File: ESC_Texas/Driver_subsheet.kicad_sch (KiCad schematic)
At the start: 24 parts, among them IC10 UCC21331CQDRQ1, Q2 IPD100N06S4, Q5 IPD100N06S4

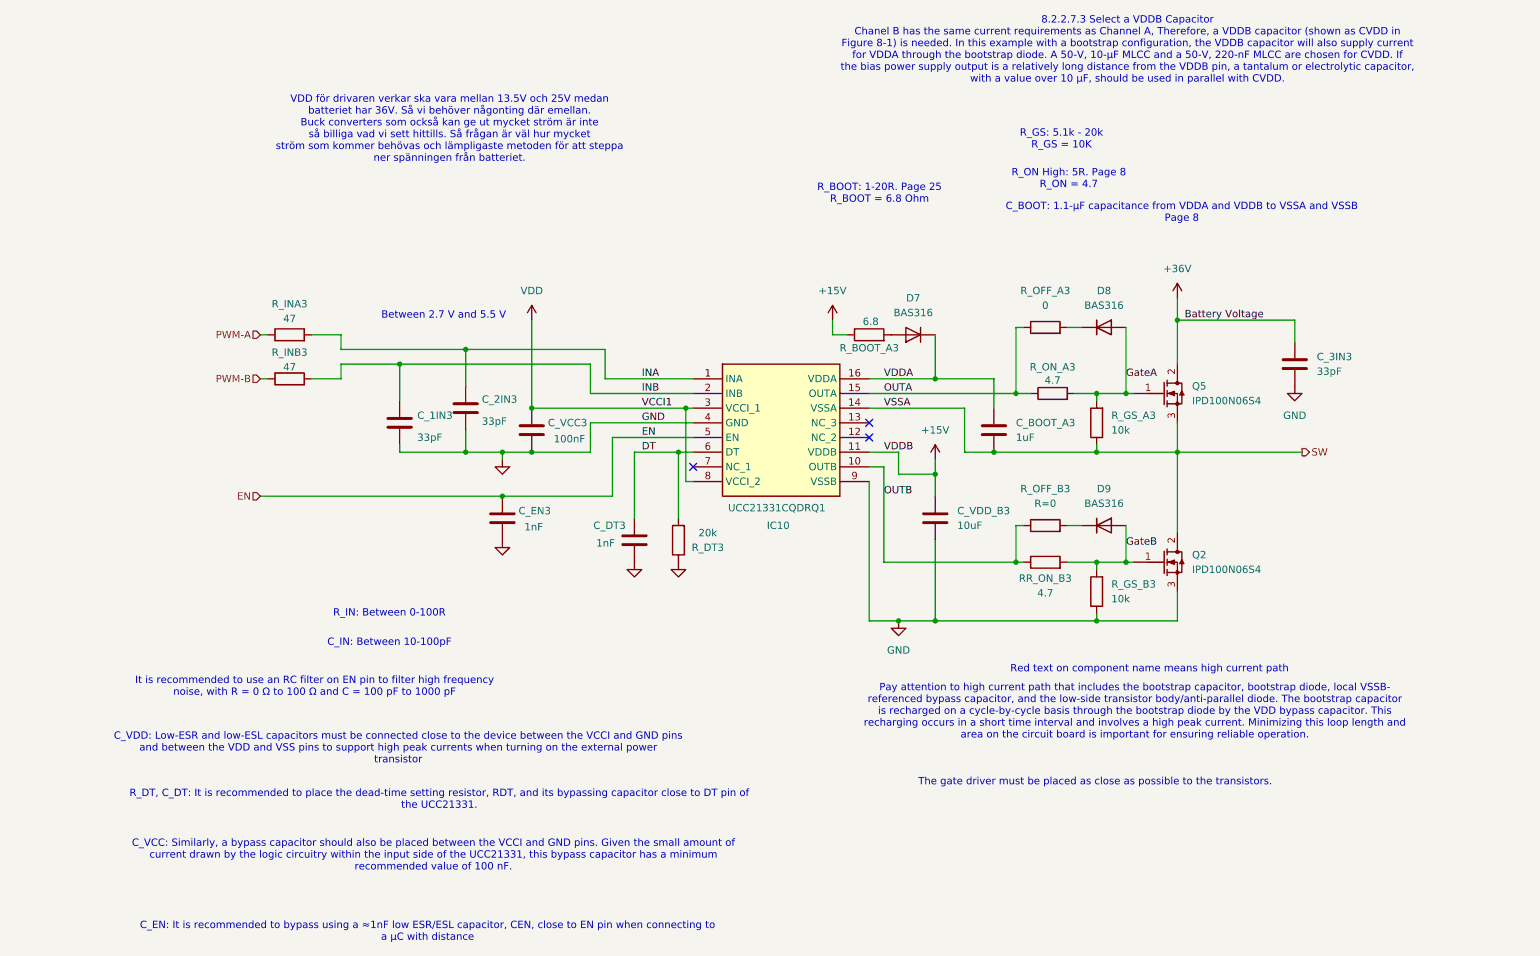
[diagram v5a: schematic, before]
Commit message: Added capacitors and more
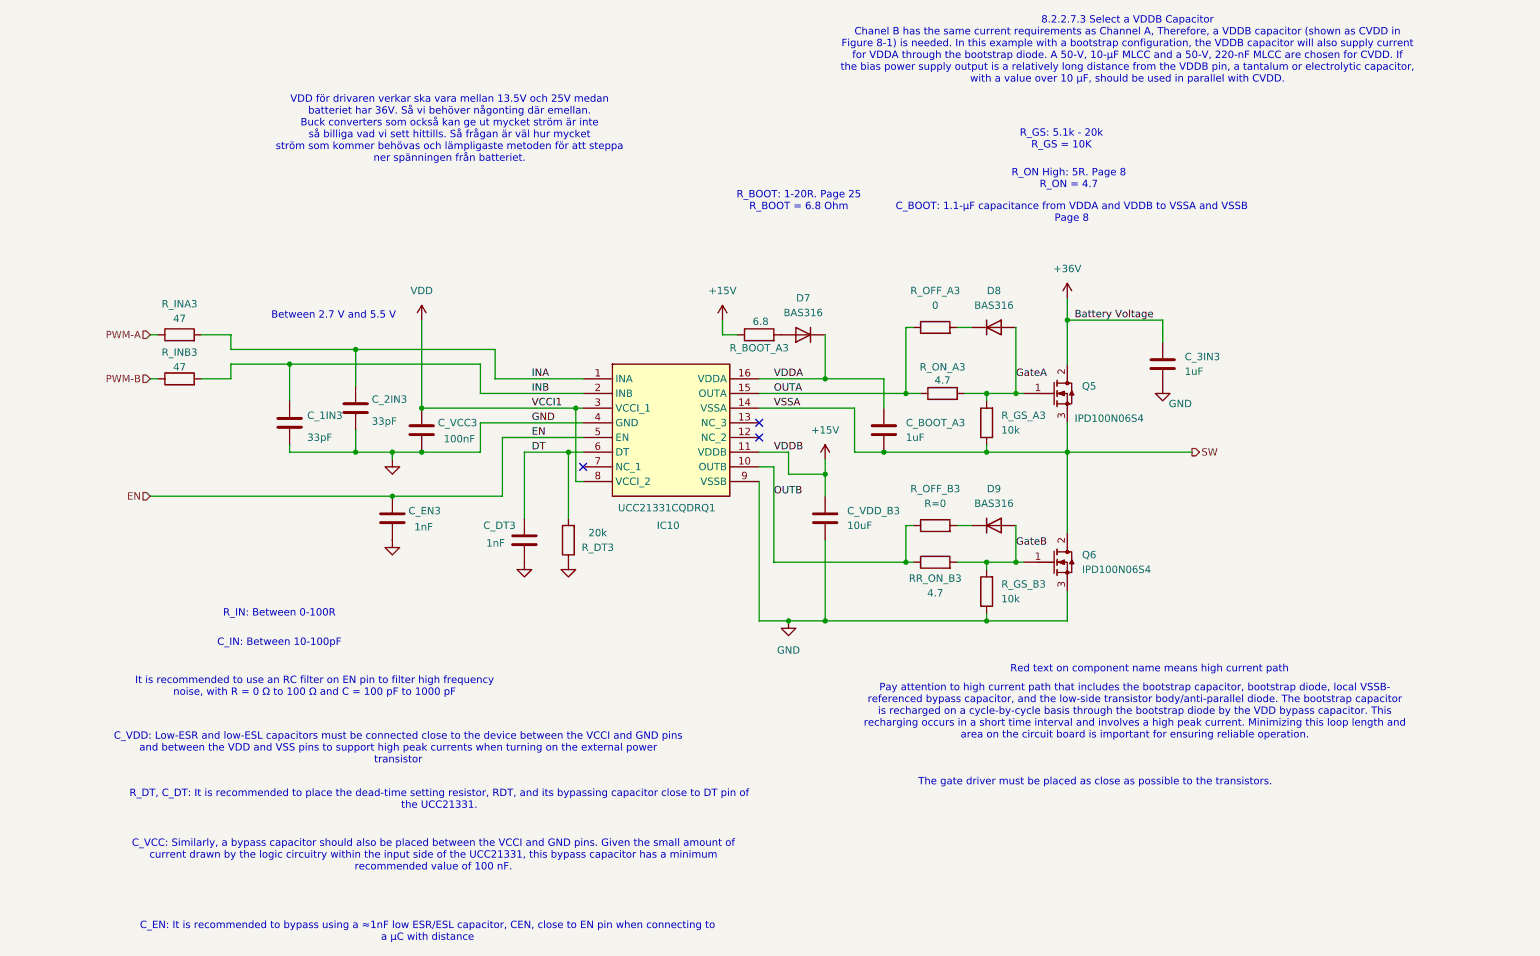
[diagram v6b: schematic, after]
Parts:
- C_3IN3: value 33pF -> 1uF
- renumbered Q2 to Q6
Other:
- moved on the sheet: C_1IN3, C_2IN3, C_3IN3, C_BOOT_A3, C_DT3, C_EN3, C_VCC3, C_VDD_B3, D7, D8, D9, IC10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

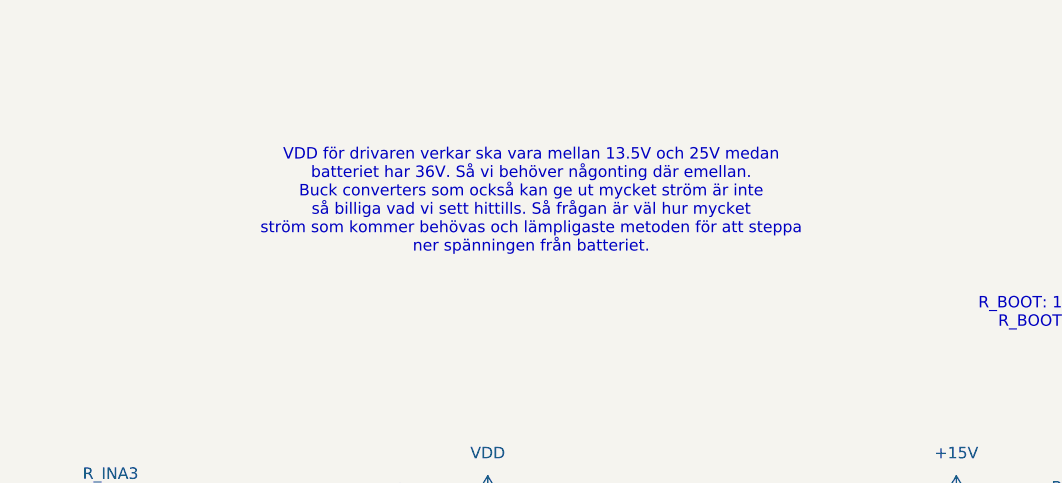
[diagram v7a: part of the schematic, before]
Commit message: Testpoints instead of hearders
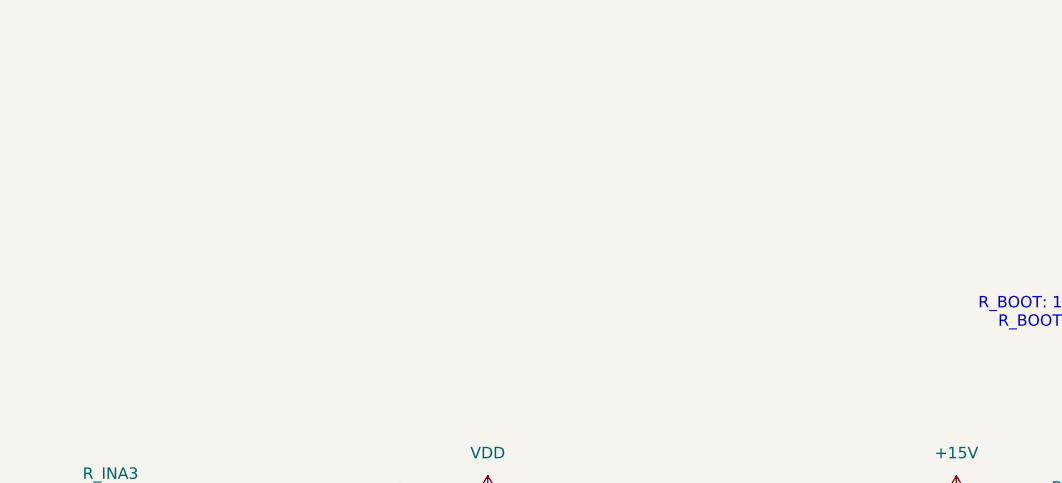
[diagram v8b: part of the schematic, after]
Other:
- note removed: "VDD för drivaren verkar ska vara mellan 13.5V och 25V medan batteriet har 36V. Så vi behöver någonting där emellan. Buck converters som också kan ge ut mycket ström är inte så billiga vad vi sett hittills. Så frågan är väl hur mycket ström som kommer behövas och lämpligaste metoden för att steppa ner spänningen från batteriet."
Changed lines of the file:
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@@
-		)
-	)
-	(text "VDD för drivaren verkar ska vara mellan 13.5V och 25V medan \nbatteriet har 36V. Så vi behöver någonting där emellan. \nBuck converters som också kan ge ut mycket ström är inte \nså billiga vad vi sett hittills. Så frågan är väl hur mycket \nström som kommer behövas och lämpligaste metoden för att steppa \nner spänningen från batteriet. "
-		(exclude_from_sim no)
-		(at 86.106 43.18 0)
-		(effects
-			(font
-				(size 1.27 1.27)
-			)
 		)
 	)
